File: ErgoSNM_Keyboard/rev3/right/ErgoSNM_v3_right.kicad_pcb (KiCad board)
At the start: 2 copper layers, 115.6 x 106.7 mm, 89 parts, among them J1 USB_C_Receptacle_USB2.0, J2 Conn_01x02, J3 Conn_01x08, J4 Conn_01x04, SW1 SW_DPDT_x2, SW2 RESET, U1 TPS61220DCK, U2 E73-2G4M08S1C, U3 RT9013-33GB, Y1 32.768kHz

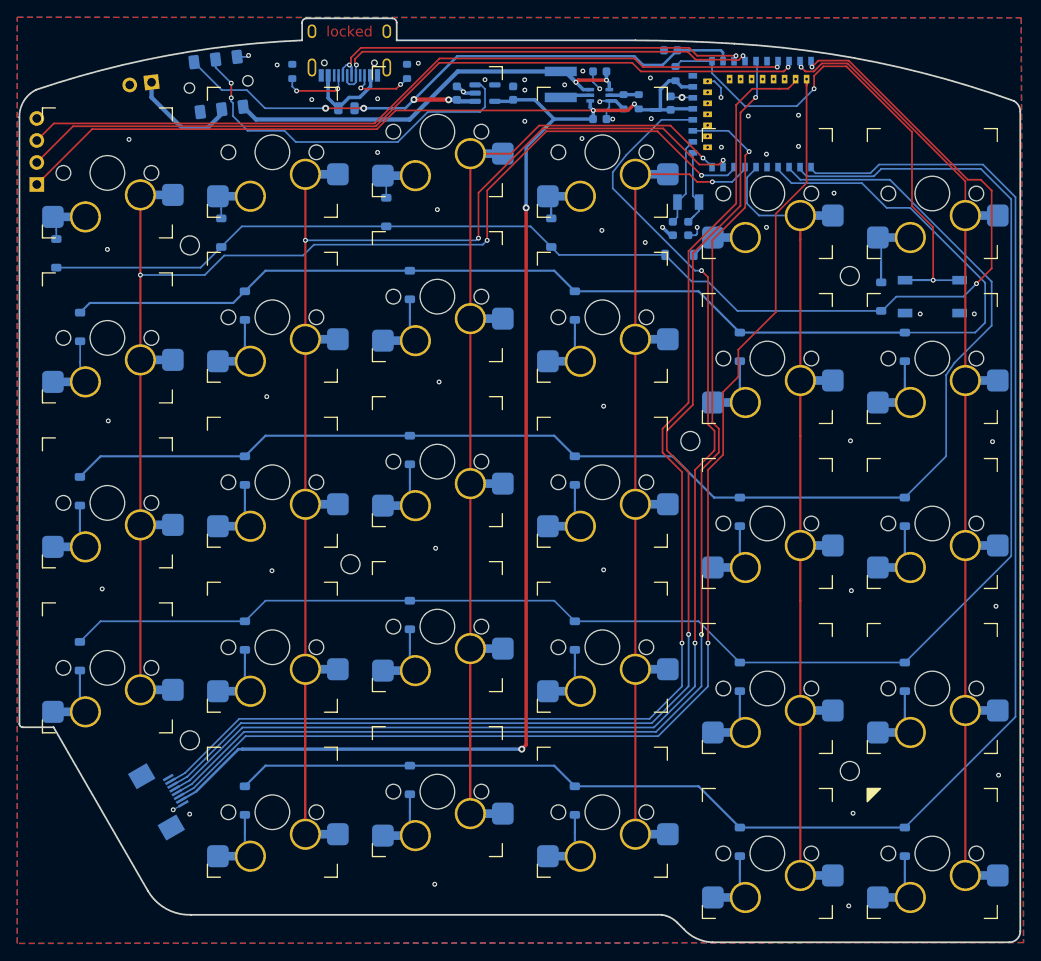
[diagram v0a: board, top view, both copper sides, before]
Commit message: Add key-matrix test pointes (2.54mm pin header)
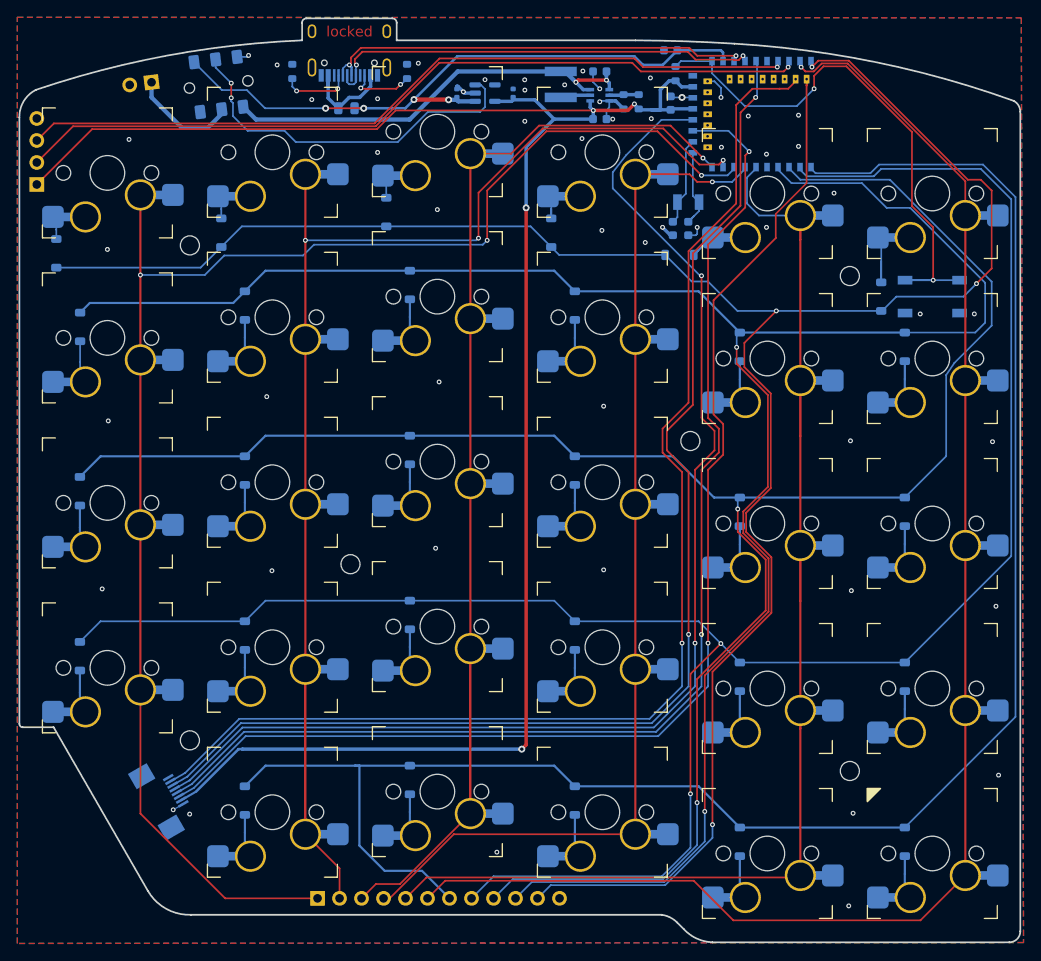
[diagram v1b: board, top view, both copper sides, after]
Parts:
- added J5: Conn_01x12, Connector_PinHeader_2.54mm:PinHeader_1x12_P2.54mm_Vertical, B.Cu at (109.0, 135.4)
- C7, C8: footprint Capacitor_SMD:C_0603_1608Metric -> Capacitor_SMD:C_0402_1005Metric
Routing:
- net ROW_0: track 153.1 -> 245.0 mm, vias 2 -> 4
- net ROW_1: track 144.2 -> 234.6 mm, vias 0 -> 2
- net ROW_2: track 158.1 -> 229.0 mm, vias 0 -> 2
- net COL_0: track 123.7 -> 190.7 mm
- net ROW_3: track 185.8 -> 238.5 mm, vias 0 -> 2
- net COL_1: track 124.7 -> 171.4 mm
- net COL_5: track 153.6 -> 192.3 mm
- net COL_2: track 108.8 -> 141.0 mm
- net ROW_4: track 184.2 -> 206.9 mm
- net COL_3: track 145.3 -> 161.9 mm
- net COL_4: track 173.8 -> 182.9 mm
- net PMW3360_SPI_CS: track 141.8 -> 142.7 mm

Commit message: Update submodule
Update submodule

Update switch footprint
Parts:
- renumbered C7 to C1, C8 to C2, C2 to C3, C1 to C4, C3 to C7, C4 to C8, D26 to D10, D3 to D11, D9 to D12, D15 to D13, D21 to D14, D27 to D15, D4 to D16, D10 to D17, D16 to D18, D22 to D19, D7 to D2, D28 to D20, D5 to D21, D11 to D22, D17 to D23, D23 to D24, D29 to D25, D6 to D26, D12 to D27, D18 to D28, D24 to D29, D13 to D3, D19 to D4, D25 to D5, D2 to D6, D8 to D7, D14 to D8, D20 to D9, J4 to J3, J3 to J4, KEY26 to KEY10, KEY3 to KEY11, KEY9 to KEY12, KEY15 to KEY13, KEY21 to KEY14, KEY27 to KEY15, KEY4 to KEY16, KEY10 to KEY17, KEY16 to KEY18, KEY22 to KEY19, KEY7 to KEY2, KEY28 to KEY20, KEY5 to KEY21, KEY11 to KEY22, KEY17 to KEY23, KEY23 to KEY24, KEY29 to KEY25, KEY6 to KEY26, KEY12 to KEY27, KEY18 to KEY28, KEY24 to KEY29, KEY13 to KEY3, KEY19 to KEY4, KEY25 to KEY5, KEY2 to KEY6, KEY8 to KEY7, KEY14 to KEY8, KEY20 to KEY9, R2 to R1, R3 to R2, R1 to R3, U3 to U1, U1 to U2, U2 to U3
